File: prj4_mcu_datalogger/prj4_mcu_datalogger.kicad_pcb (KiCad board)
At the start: 2 copper layers, 53.3 x 34.9 mm, 31 parts, among them J1 Conn_01x04_Pin, J2 Conn_01x04_Pin, J3 Conn_01x09_Pin, J4 Conn_02x03_Odd_Even, U1 DS1337S+, U2 ATMEGA328P-AU, U3 24LC1025, U4 24LC1025, Y1 32.768 KHz, Y2 16 MHz

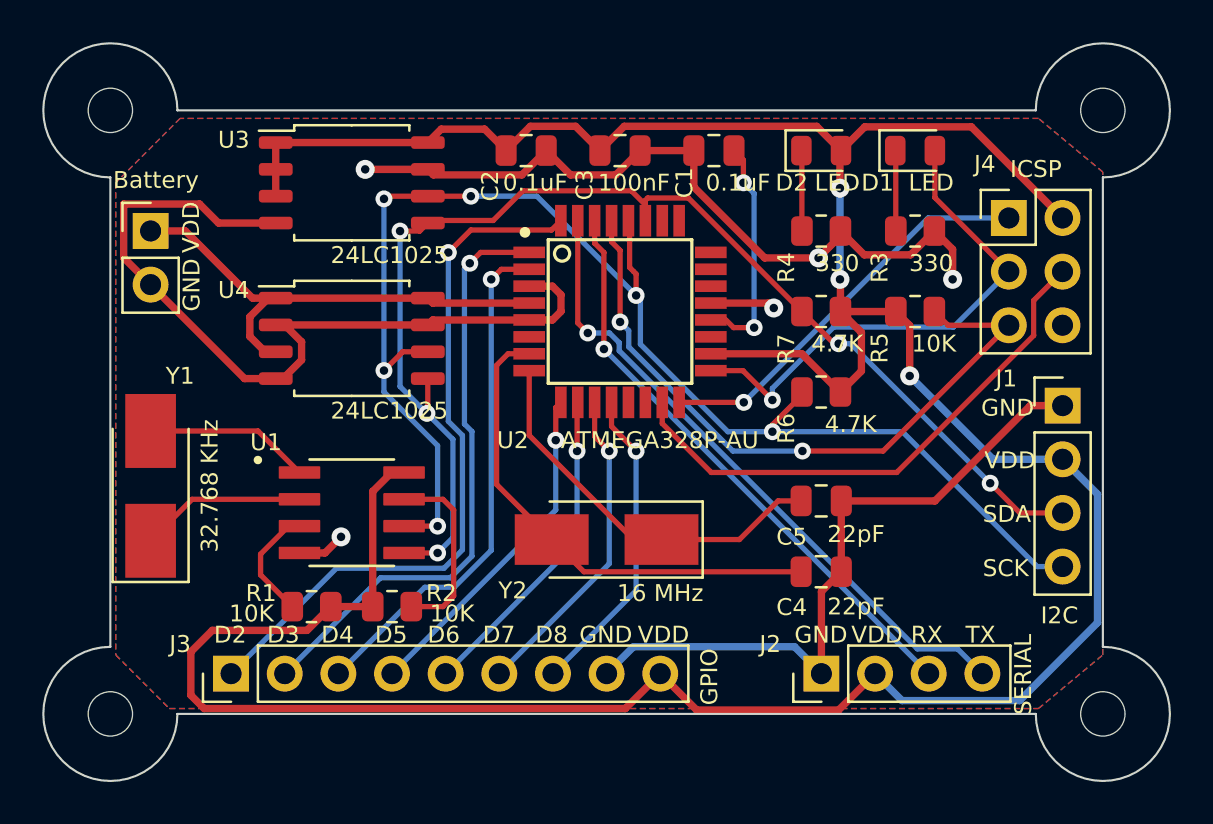
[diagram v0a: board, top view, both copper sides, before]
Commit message: Rimosse tutte le connessioni tra i componenti
Feat: eliminate tracce e via
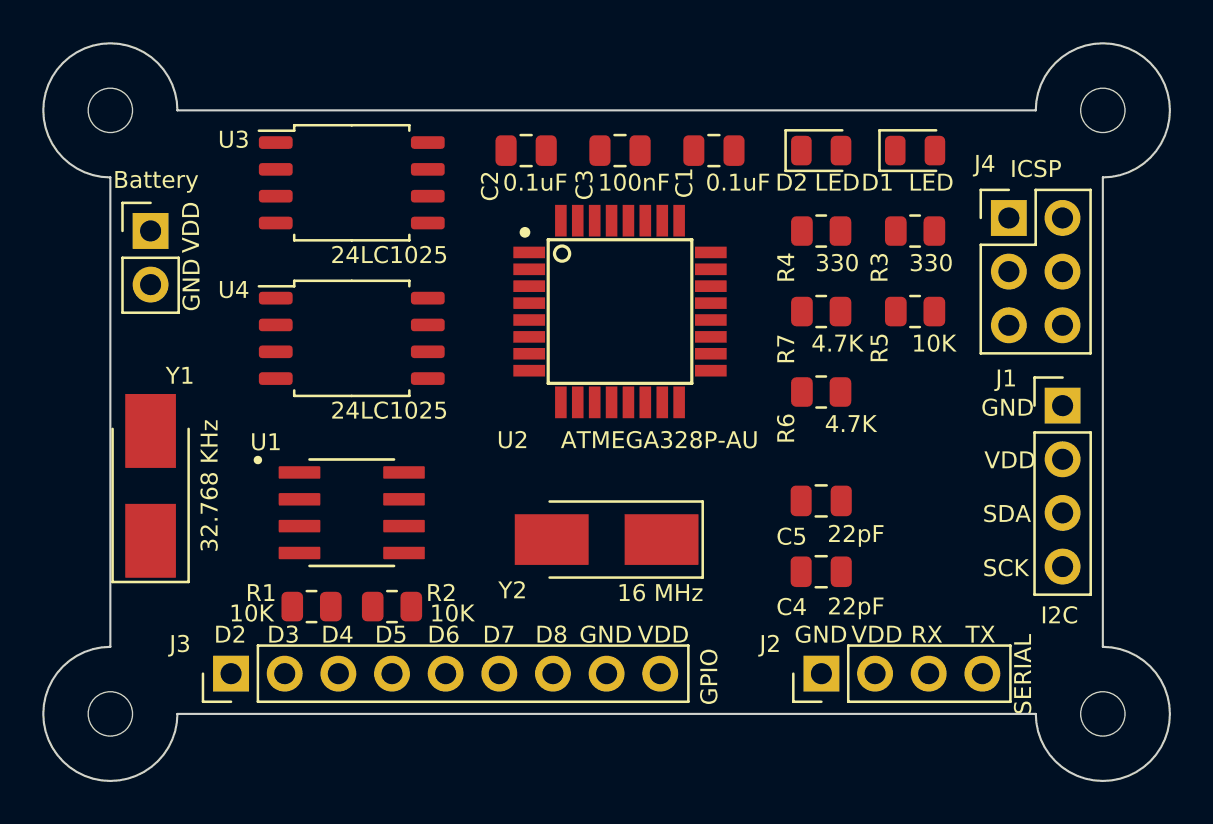
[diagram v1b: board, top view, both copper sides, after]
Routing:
- net /Vcc: track 176.6 -> 0.00 mm, vias 3 -> 0
- net GND: track 113.5 -> 0.00 mm, vias 5 -> 0
- net /SCL: track 67.4 -> 0.00 mm, vias 6 -> 0
- net /SDA: track 60.2 -> 0.00 mm, vias 5 -> 0
- net /D2: track 33.7 -> 0.00 mm, vias 1 -> 0
- net /RESET: track 32.6 -> 0.00 mm, vias 2 -> 0
- net /TX: track 31.1 -> 0.00 mm, vias 1 -> 0
- net /D3: track 28.3 -> 0.00 mm, vias 1 -> 0
- net /RX: track 28.0 -> 0.00 mm, vias 1 -> 0
- net /MOSI: track 25.8 -> 0.00 mm
- net /SCK: track 24.7 -> 0.00 mm, vias 1 -> 0
- net /D4: track 24.5 -> 0.00 mm, vias 1 -> 0
- net Net-(U2-PB6): track 23.5 -> 0.00 mm
- net /MISO: track 19.2 -> 0.00 mm, vias 1 -> 0
- net Net-(U2-PB7): track 18.7 -> 0.00 mm
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- removed copper zone on F.Cu, net /Vcc
- removed copper zone on B.Cu, net GND

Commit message: Create connessioni mediante Freerouting
Feat: creato routing automatico
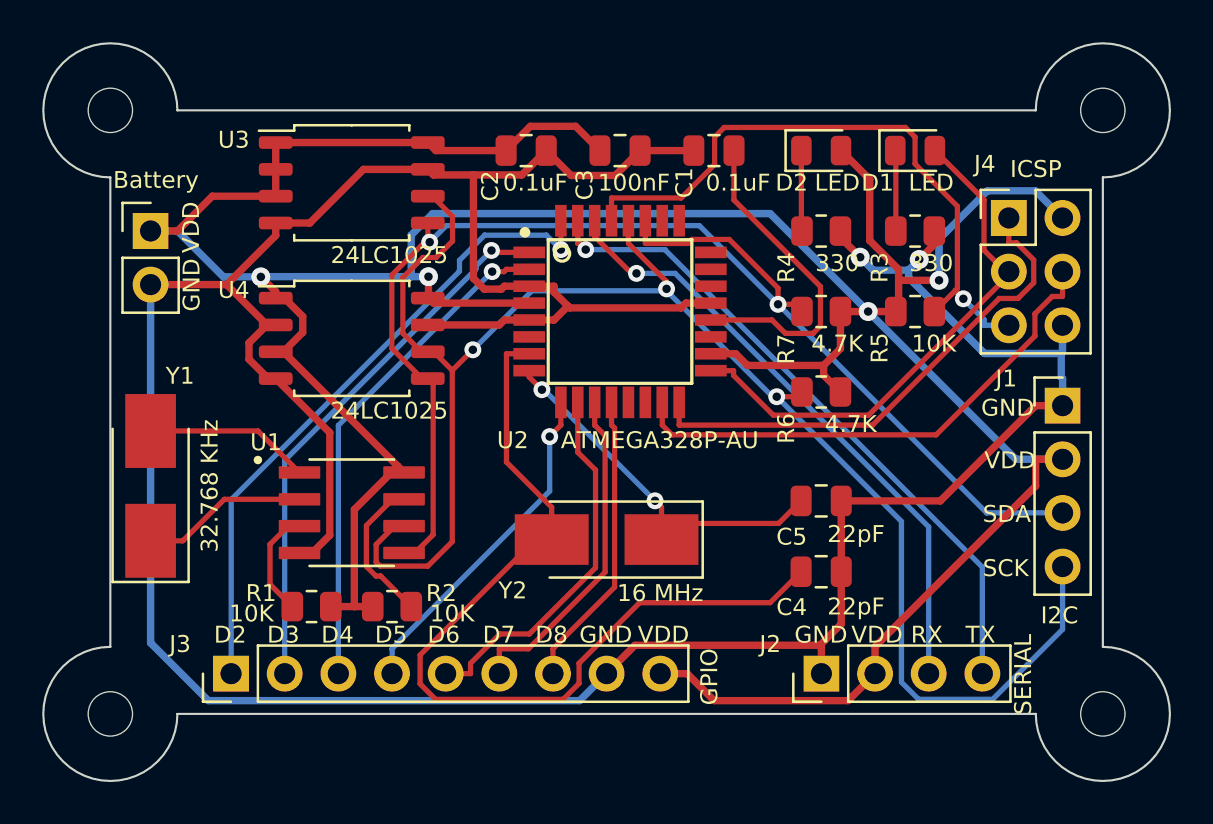
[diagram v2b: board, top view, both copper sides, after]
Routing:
- net /Vcc: track 0.00 -> 165.0 mm, vias 0 -> 4
- net GND: track 0.00 -> 162.3 mm, vias 0 -> 2
- net /SCL: track 0.00 -> 78.9 mm, vias 0 -> 3
- net /SDA: track 0.00 -> 64.7 mm, vias 0 -> 2
- net Net-(U2-PB6): track 0.00 -> 42.3 mm
- net /TX: track 0.00 -> 31.6 mm, vias 0 -> 1
- net /D2: track 0.00 -> 31.0 mm, vias 0 -> 1
- net /RESET: track 0.00 -> 30.7 mm, vias 0 -> 1
- net /RX: track 0.00 -> 29.2 mm, vias 0 -> 1
- net /D3: track 0.00 -> 25.9 mm, vias 0 -> 1
- net /SCK: track 0.00 -> 25.2 mm
- net /MOSI: track 0.00 -> 24.7 mm
- net /MISO: track 0.00 -> 24.4 mm
- net /D4: track 0.00 -> 23.8 mm, vias 0 -> 1
- net Net-(U2-PB7): track 0.00 -> 17.7 mm, vias 0 -> 2
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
